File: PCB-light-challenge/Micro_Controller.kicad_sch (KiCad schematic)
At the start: 1 part

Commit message: Batterij charger foorprint en symbol toegevoegd, BMS schema getekend , LDO symbol en footprint toegevoegd
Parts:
- U-PICO1: footprint (none) -> custom_footprint_pico:Pico_light challenge
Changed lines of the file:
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@@
       (effects (font (size 1.27 1.27)))
     )
-    (property "Footprint" "" (at 128.27 74.93 0)
+    (property "Footprint" "custom_footprint_pico:Pico_light challenge" (at 128.27 74.93 0)
       (effects (font (size 1.27 1.27)) hide)
     )

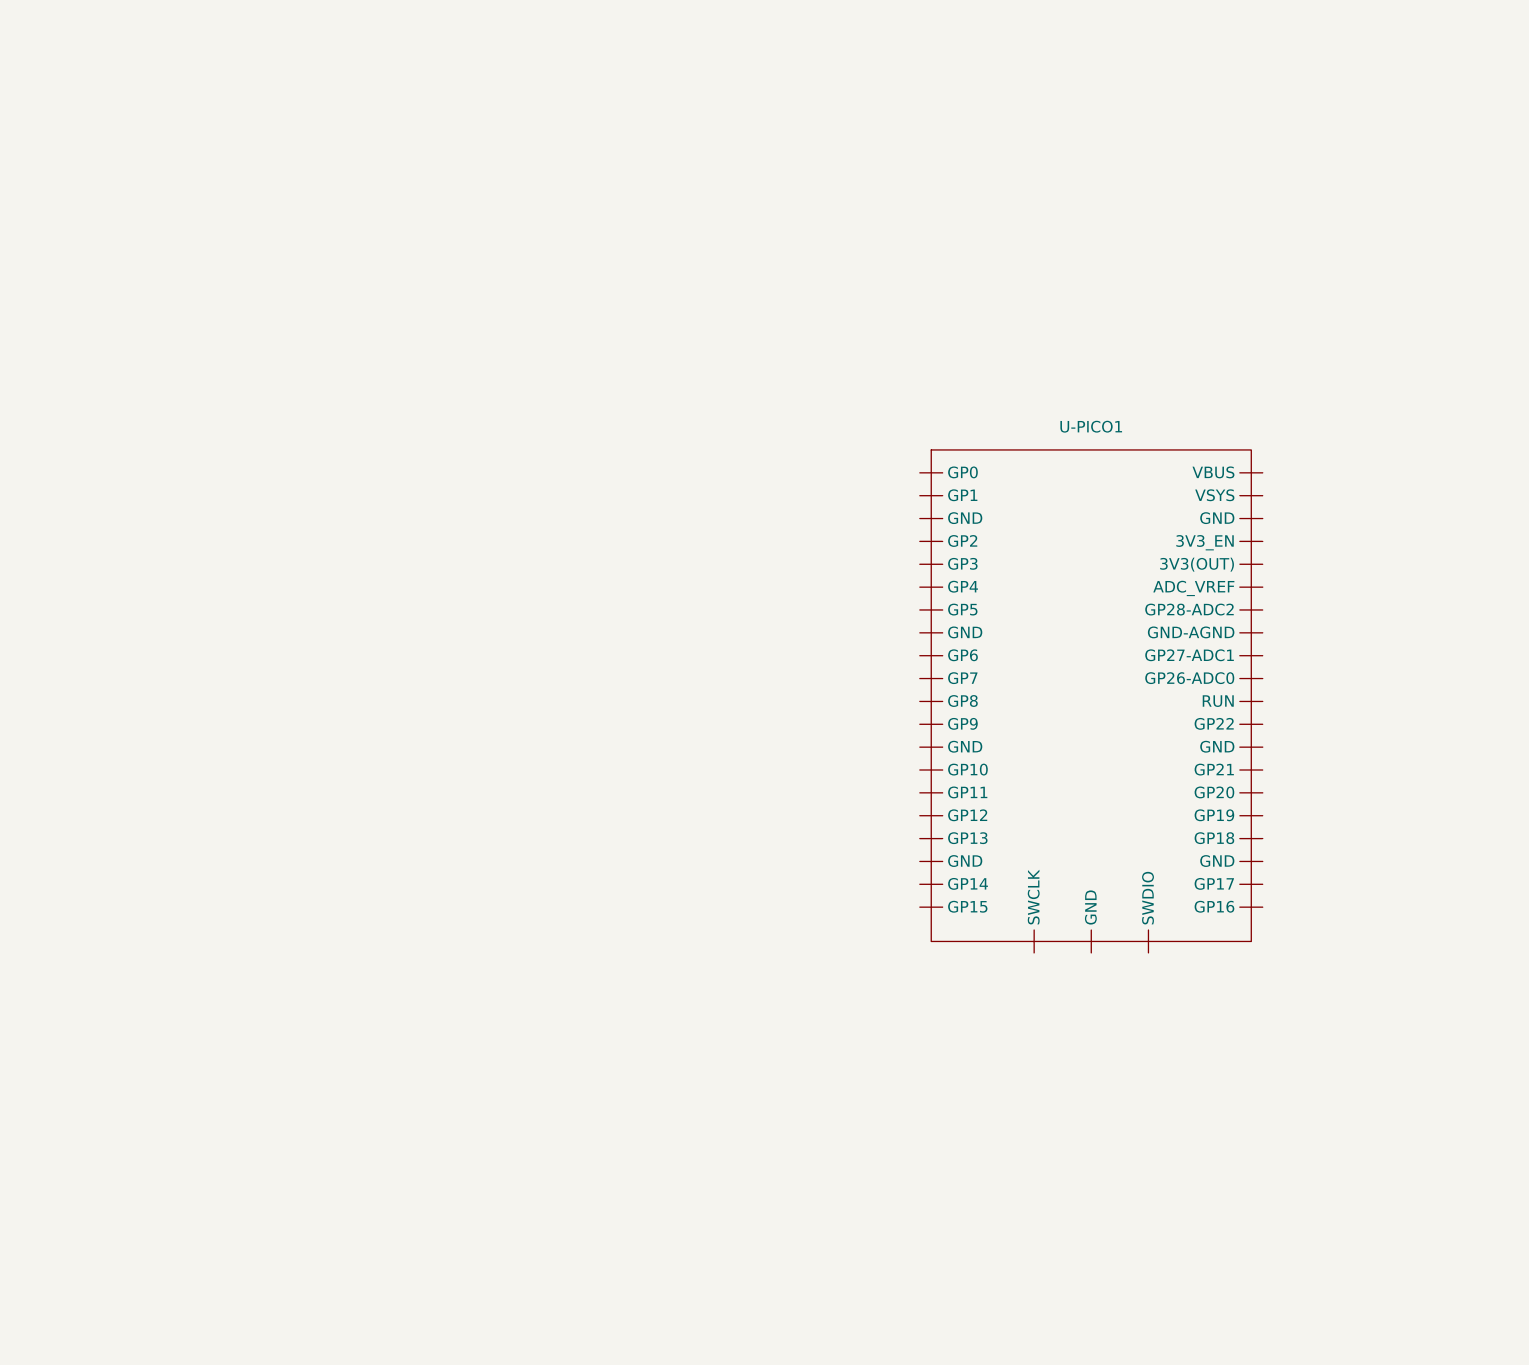
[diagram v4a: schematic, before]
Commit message: RP2040  pinout toegevoegd   met naam
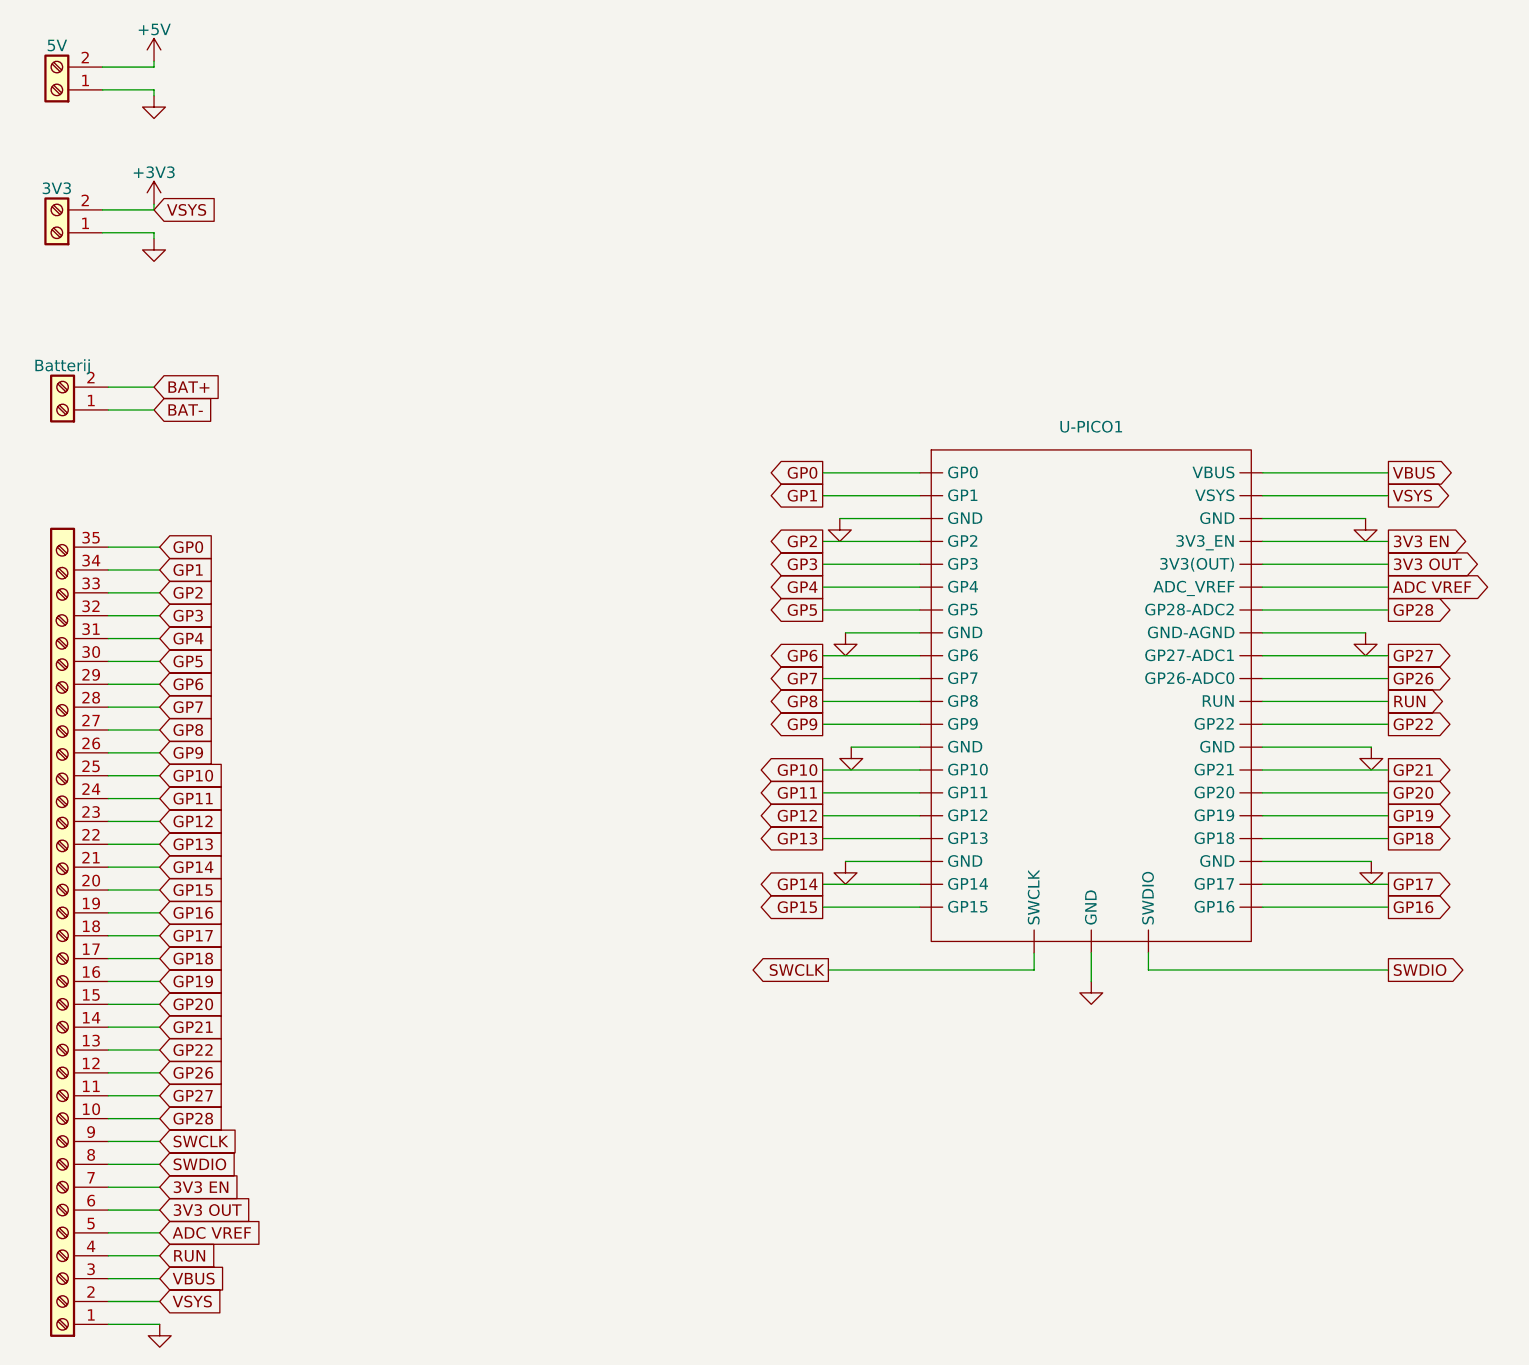
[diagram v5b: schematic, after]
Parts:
- added 3V3, 5V, Batterij: Screw_Terminal_01x02, Connector_PinHeader_2.54mm:PinHeader_1x02_P2.54mm_Horizontal, symbol Connector:Screw_Terminal_01x02
- added J2: Screw_Terminal_01x20, Connector_PinHeader_2.54mm:PinHeader_1x35_P2.54mm_Horizontal, symbol Connector:Screw_Terminal_01x20
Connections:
- net VBUS: now reaches U-PICO1. (VSYS)
- net VBUS: now also J2.3 (Pin_3)
- new net +3V3: 3V3.2 (Pin_2), J2.2 (Pin_2), U-PICO1. (VSYS)
- new net +5V: 5V.2 (Pin_2)
- new net 3V3 EN: J2.7 (Pin_7), U-PICO1. (VSYS)
- new net 3V3 OUT: J2.6 (Pin_6), U-PICO1. (VSYS)
- new net ADC VREF: J2.5 (Pin_5), U-PICO1. (VSYS)
- new net BAT+: Batterij.2 (Pin_2)
- new net BAT-: Batterij.1 (Pin_1)
- new net GND: 3V3.1 (Pin_1), 5V.1 (Pin_1), J2.1 (Pin_1), U-PICO1. (VSYS)
- new net GP0: J2.35 (Pin_35), U-PICO1. (VSYS)
- new net GP1: J2.34 (Pin_34), U-PICO1. (VSYS)
- new net GP10: J2.25 (Pin_25), U-PICO1. (VSYS)
- new net GP11: J2.24 (Pin_24), U-PICO1. (VSYS)
- new net GP12: J2.23 (Pin_23), U-PICO1. (VSYS)
- new net GP13: J2.22 (Pin_22), U-PICO1. (VSYS)
- new net GP14: J2.21 (Pin_21), U-PICO1. (VSYS)
- new net GP15: J2.20 (Pin_20), U-PICO1. (VSYS)
- new net GP16: J2.19 (Pin_19), U-PICO1. (VSYS)
- new net GP17: J2.18 (Pin_18), U-PICO1. (VSYS)
- new net GP18: J2.17 (Pin_17), U-PICO1. (VSYS)
- new net GP19: J2.16 (Pin_16), U-PICO1. (VSYS)
- new net GP2: J2.33 (Pin_33), U-PICO1. (VSYS)
- new net GP20: J2.15 (Pin_15), U-PICO1. (VSYS)
- new net GP21: J2.14 (Pin_14), U-PICO1. (VSYS)
- new net GP22: J2.13 (Pin_13), U-PICO1. (VSYS)
- new net GP26: J2.12 (Pin_12), U-PICO1. (VSYS)
- new net GP27: J2.11 (Pin_11), U-PICO1. (VSYS)
- new net GP28: J2.10 (Pin_10), U-PICO1. (VSYS)
- new net GP3: J2.32 (Pin_32), U-PICO1. (VSYS)
- new net GP4: J2.31 (Pin_31), U-PICO1. (VSYS)
- new net GP5: J2.30 (Pin_30), U-PICO1. (VSYS)
- new net GP6: J2.29, U-PICO1. (VSYS)
- new net GP7: J2.28 (Pin_28), U-PICO1. (VSYS)
- new net GP8: J2.27 (Pin_27), U-PICO1. (VSYS)
- new net GP9: J2.26 (Pin_26), U-PICO1. (VSYS)
- new net RUN: J2.4 (Pin_4), U-PICO1. (VSYS)
- new net SWCLK: J2.9 (Pin_9), U-PICO1. (VSYS)
- new net SWDIO: J2.8 (Pin_8), U-PICO1. (VSYS)
